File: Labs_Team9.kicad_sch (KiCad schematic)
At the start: 51 parts, among them J1 Conn_02x04_Counter_Clockwise, J2 Conn_01x03_Pin, J3 Conn_01x04_Pin, J4 Conn_01x04_Pin, J5 USB_C_Receptacle_PowerOnly_6P, SW1 SW_Push, SW2 SW_Push, SW3 SW_Push, SW4 SW_Push, SW5 SW_Push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

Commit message: lab5: add part of the schematic
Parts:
- removed D1, D2, D3, D4: LED, LED_SMD:LED_1206_3216Metric_Pad1.42x1.75mm_HandSolder, symbol Device:LED
- removed J4: Conn_01x04_Pin, Connector_PinHeader_2.54mm:PinHeader_1x04_P2.54mm_Vertical, symbol Connector:Conn_01x04_Pin
- removed R10, R7, R8, R9: 10 kOhm, Resistor_SMD:R_1206_3216Metric_Pad1.30x1.75mm_HandSolder, symbol Device:R
- removed R5, R6: 680 Ohm, Resistor_SMD:R_1206_3216Metric_Pad1.30x1.75mm_HandSolder, symbol Device:R
- removed RV1, RV2, RV3: R_Potentiometer, Potentiometer_THT:Potentiometer_Bourns_3339P_Vertical_HandSoldering, symbol Device:R_Potentiometer
- removed SW3, SW4, SW5, SW6: SW_Push, Buttons_Switches_THT:SW_PUSH_6mm, symbol Switch:SW_Push
- added U3: SCD40-D-R2, Sensor:Sensirion_SCD4x-1EP_10.1x10.1mm_P1.25mm_EP4.8x4.8mm, symbol Sensor_Gas:SCD40-D-R2
- R3: value 510 Ohm -> 10 kOhm
- R4: value 680 Ohm -> 10 kOhm
- renumbered R13 to R10, R14 to R11, R11 to R5, R12 to R6, R15 to R8, R16 to R9
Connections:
- net Led_Blue is gone; now on net I2C2_SCL: U1.41 (PA8)
- net USERB4 is gone; now on net I2C2_SDA: U1.40 (PC9)
- net +3.3V: now also R3.1, R4.1, U3.19 (VDD), U3.7 (VDD)
- net GND: now also U3.20 (GND), U3.21 (GND), U3.6 (GND)
- net I2C2_SDA: now reaches R3.2
- net I2C2_SDA: now also U3.10 (SDA)
- net I2C2_SCL: now reaches R4.2
- net I2C2_SCL: now also U3.9 (SCL)
- net ADC_MCU_1: no longer names the net of U1.25 (PC5)
- net ADC_MCU_2: no longer names the net of U1.26 (PB0)
- net ADC_MCU_3: no longer names the net of U1.27 (PB1)
- net Led_Green: no longer names the net of U1.59 (PB7)
- net Led_Green: no longer R3.1
- net Led_Orange: no longer names the net of U1.58 (PB6)
- net Led_Orange: no longer R4.1
- net Led_Red: no longer names the net of U1.50 (PA15)
- net SPI_MISO: no longer names the net of U1.22 (PA6)
- net SPI_MOSI: no longer names the net of U1.23 (PA7)
- net SPI_NSS: no longer names the net of U1.20 (PA4)
- net SPI_SCK: no longer names the net of U1.21 (PA5)
- net USERB1: no longer names the net of U1.8 (PC0)
- net USERB2: no longer names the net of U1.9 (PC1)
- net USERB3: no longer names the net of U1.39 (PC8)
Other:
- moved on the sheet: C1, C2, C3, C4, C5, C6, C7, J1, J2, J3, R5, R6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

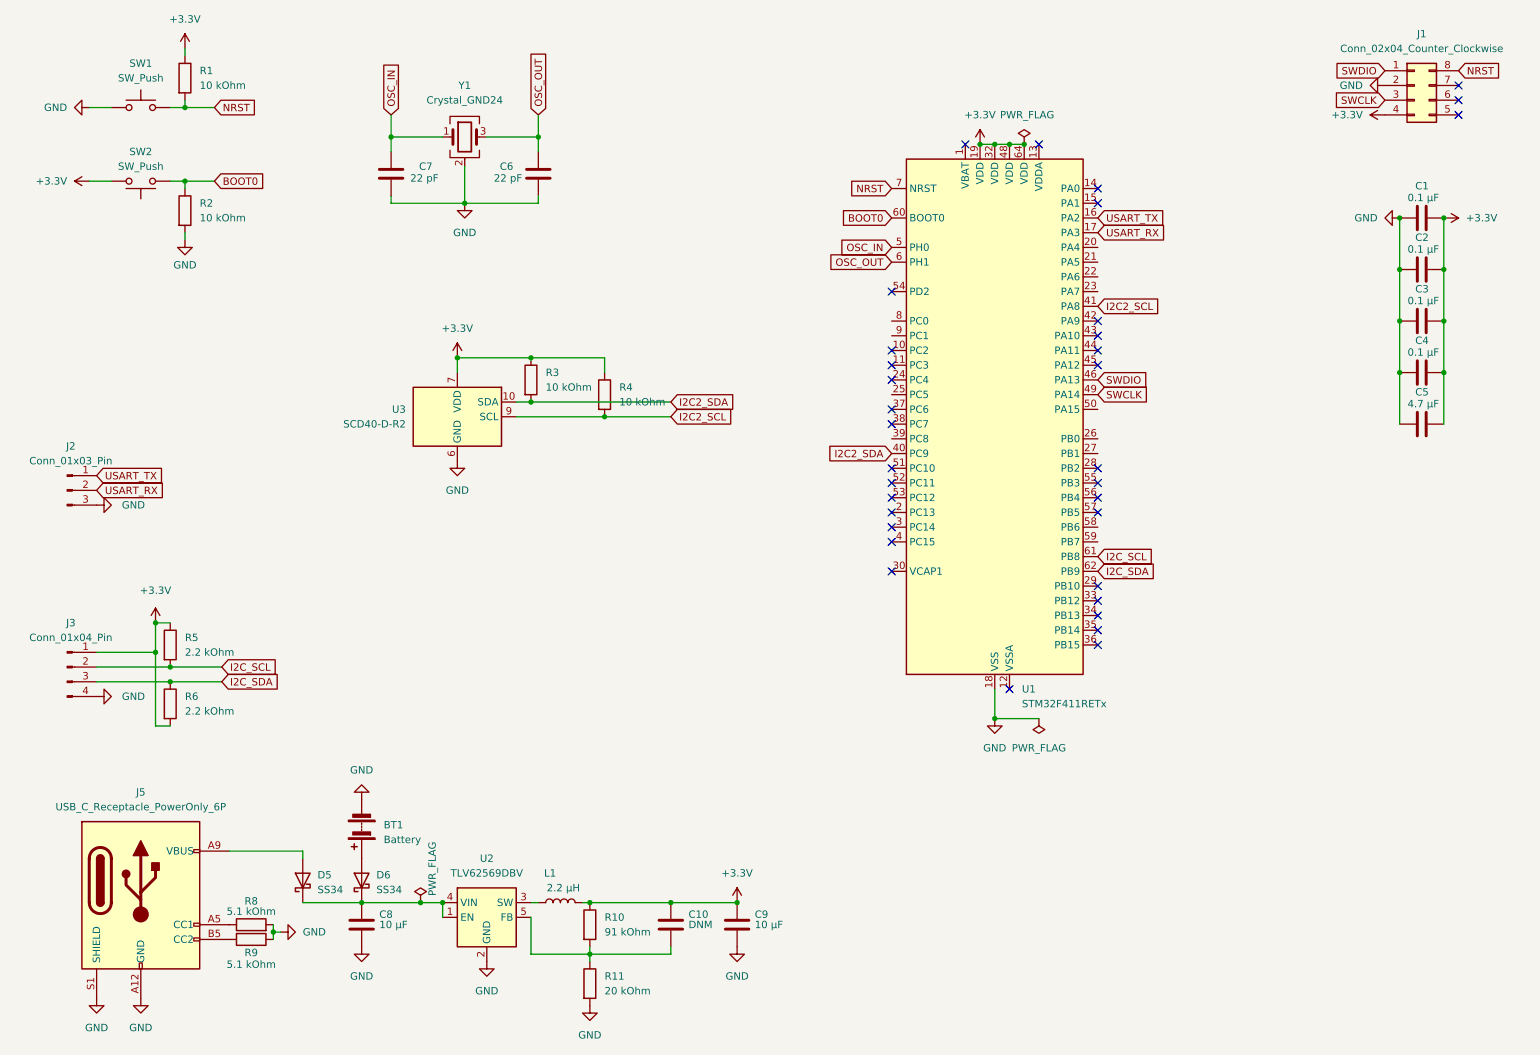
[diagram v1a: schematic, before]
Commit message: lab5: add full schematic
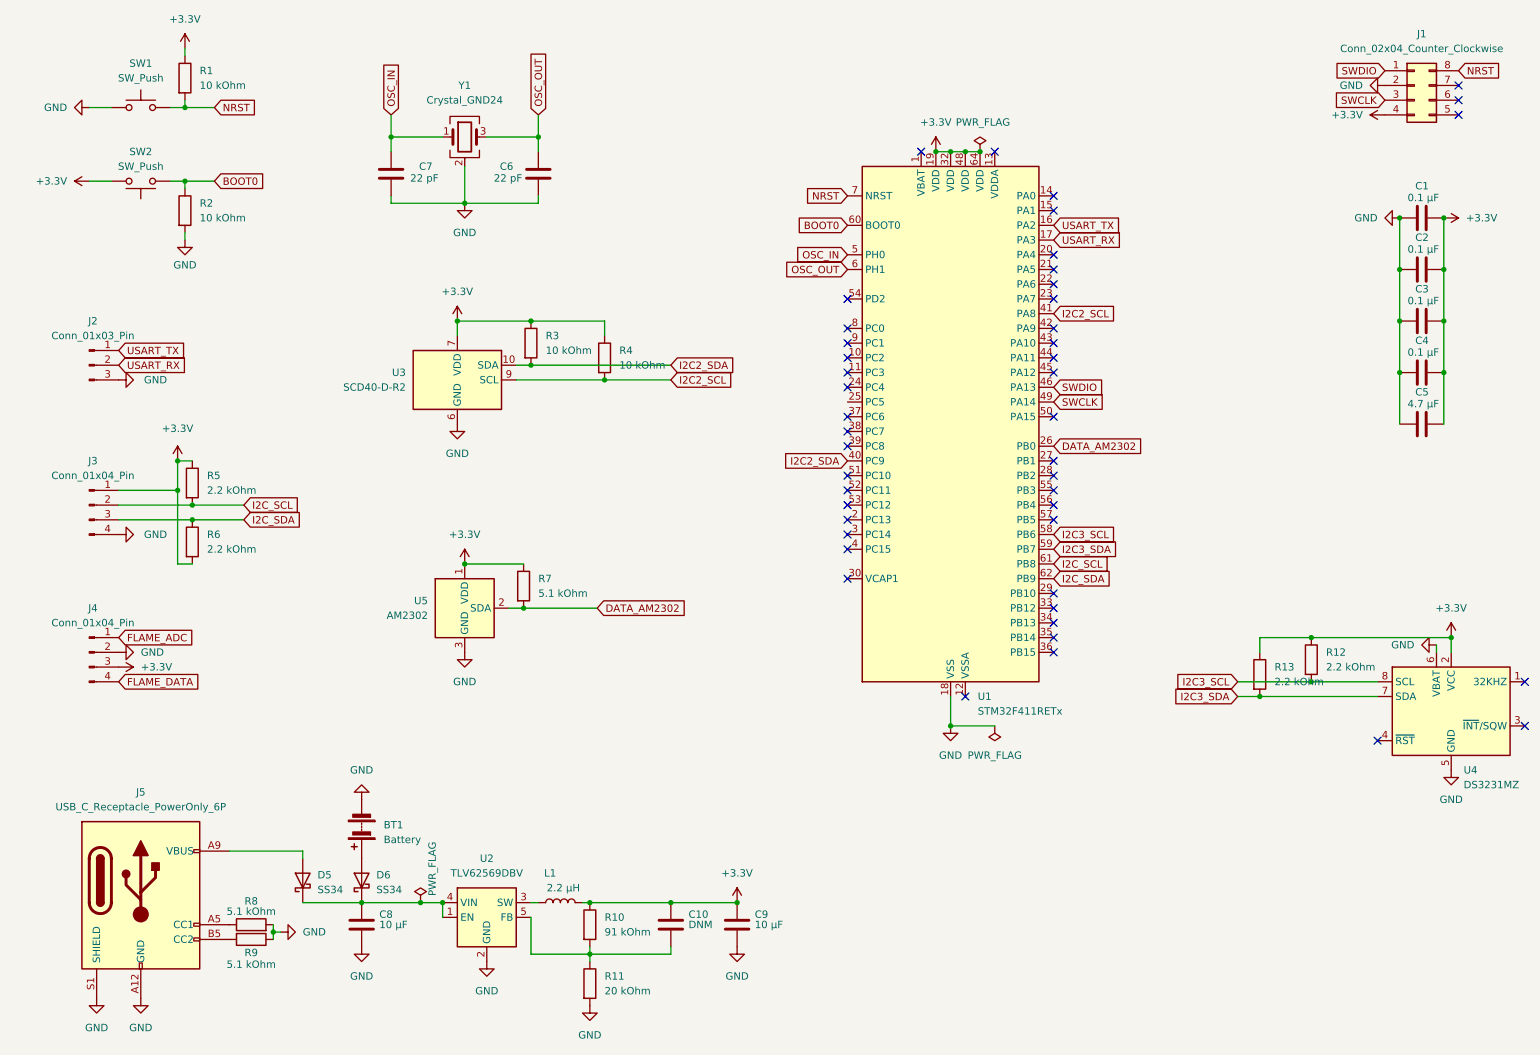
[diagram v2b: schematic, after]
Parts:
- added J4: Conn_01x04_Pin, Connector_PinHeader_2.54mm:PinHeader_1x04_P2.54mm_Vertical, symbol Connector:Conn_01x04_Pin
- added R12, R13: 2.2 kOhm, Resistor_SMD:R_1206_3216Metric_Pad1.30x1.75mm_HandSolder, symbol Device:R
- added R7: 5.1 kOhm, Resistor_SMD:R_1206_3216Metric_Pad1.30x1.75mm_HandSolder, symbol Device:R
- added U4: DS3231MZ, Package_SO:SOIC-8_3.9x4.9mm_P1.27mm, symbol Timer_RTC:DS3231MZ
- added U5: AM2302, Sensor:ASAIR_AM2302_P2.54mm_Lead2.75mm_TabDown, symbol Sensor:AM2302
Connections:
- net +3.3V: now also J4.3 (Pin_3), R12.1, R13.1, R7.1, U4.2 (VCC), U5.1 (VDD)
- net GND: now also J4.2 (Pin_2), U4.5 (GND), U4.6 (VBAT), U5.3 (GND), U5.4 (GND)
- net DATA_AM2302: now reaches U1.26 (PB0)
- net DATA_AM2302: now also R7.2, U5.2 (SDA)
- net I2C3_SCL: now reaches U1.58 (PB6)
- net I2C3_SCL: now also R12.2, U4.8 (SCL)
- net I2C3_SDA: now reaches U1.59 (PB7)
- net I2C3_SDA: now also R13.2, U4.7 (SDA)
- new net FLAME_ADC: J4.1 (Pin_1)
- new net FLAME_DATA: J4.4 (Pin_4)
- no-connect marks 34 -> 46
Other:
- moved on the sheet: J2, J3, R3, R4, R5, R6, U1, U3

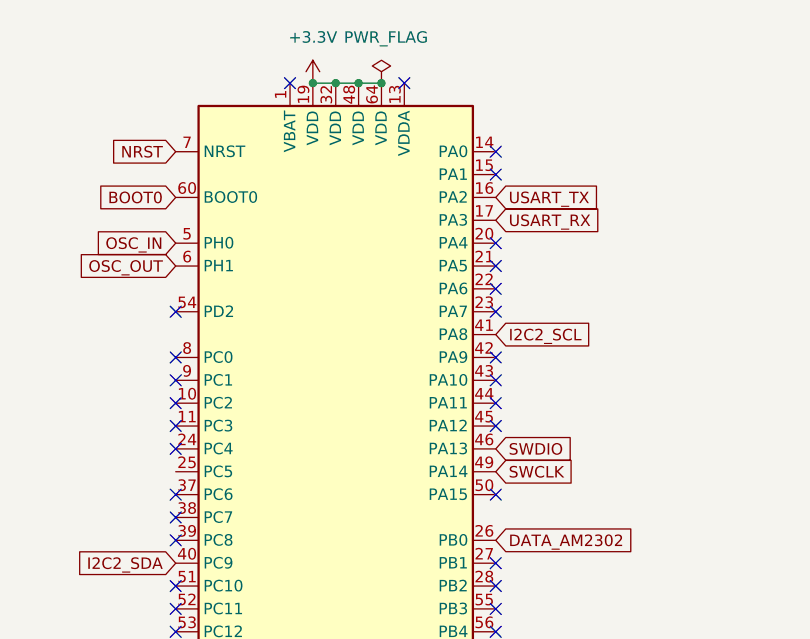
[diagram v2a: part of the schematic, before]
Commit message: lab5: add full tracing
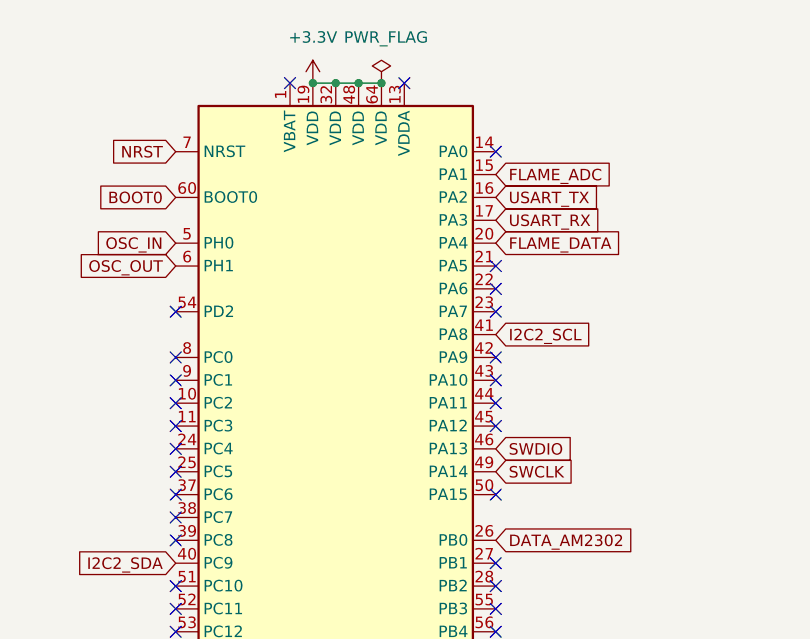
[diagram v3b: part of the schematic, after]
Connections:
- net FLAME_ADC: now also U1.15 (PA1)
- net FLAME_DATA: now also U1.20 (PA4)
- no-connect marks 46 -> 45
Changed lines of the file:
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@@
+	)
+	(no_connect
+		(at 160.02 82.55)
 	)
 	(no_connect
@@
 	)
 	(no_connect
-		(at 195.58 57.15)
-	)
-	(no_connect
 		(at 195.58 77.47)
 	)
@@
 	)
 	(no_connect
-		(at 195.58 49.53)
-	)
-	(no_connect
 		(at 160.02 113.03)
 	)
@@
 		)
 	)
+	(global_label "FLAME_DATA"
+		(shape input)
+		(at 195.58 57.15 0)
+		(fields_autoplaced yes)
+		(effects
+			(font
+				(size 1.27 1.27)
+			)
+			(justify left)
+		)
+		(property "Intersheetrefs" "${INTERSHEET_REFS}"
+			(at 209.7533 57.15 0)
+			(effects
+				(font
+					(size 1.27 1.27)
+				)
+				(justify left)
+				(hide yes)
+			)
+		)
+	)
 	(global_label "BOOT0"
 		(shape input)
@@
 			(effects
 				(font
+					(size 1.27 1.27)
+				)
+				(justify left)
+				(hide yes)
+			)
+		)
+	)
+	(global_label "FLAME_ADC"
+		(shape input)
+		(at 195.58 49.53 0)
+		(fields_autoplaced yes)
+		(effects
+			(font
+				(size 1.27 1.27)
+			)
+			(justify left)
+		)
+		(property "Intersheetrefs" "${INTERSHEET_REFS}"
+			(at 208.9671 49.53 0)
+			(effects
+				(font
